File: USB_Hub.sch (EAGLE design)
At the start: 53 parts, among them CON1 USB-ZX62, CON2 USB-5075AR-04-WH, CON3 USB-5075AR-04-WH, CON4 USB-5075AR-04-WH, CON5 USB-5075AR-04-WH, IC1 UPC720115, IC2 AP22652, J1 VBUS, J2 BUS/SELF, SW1 RESET, X1 24MHz

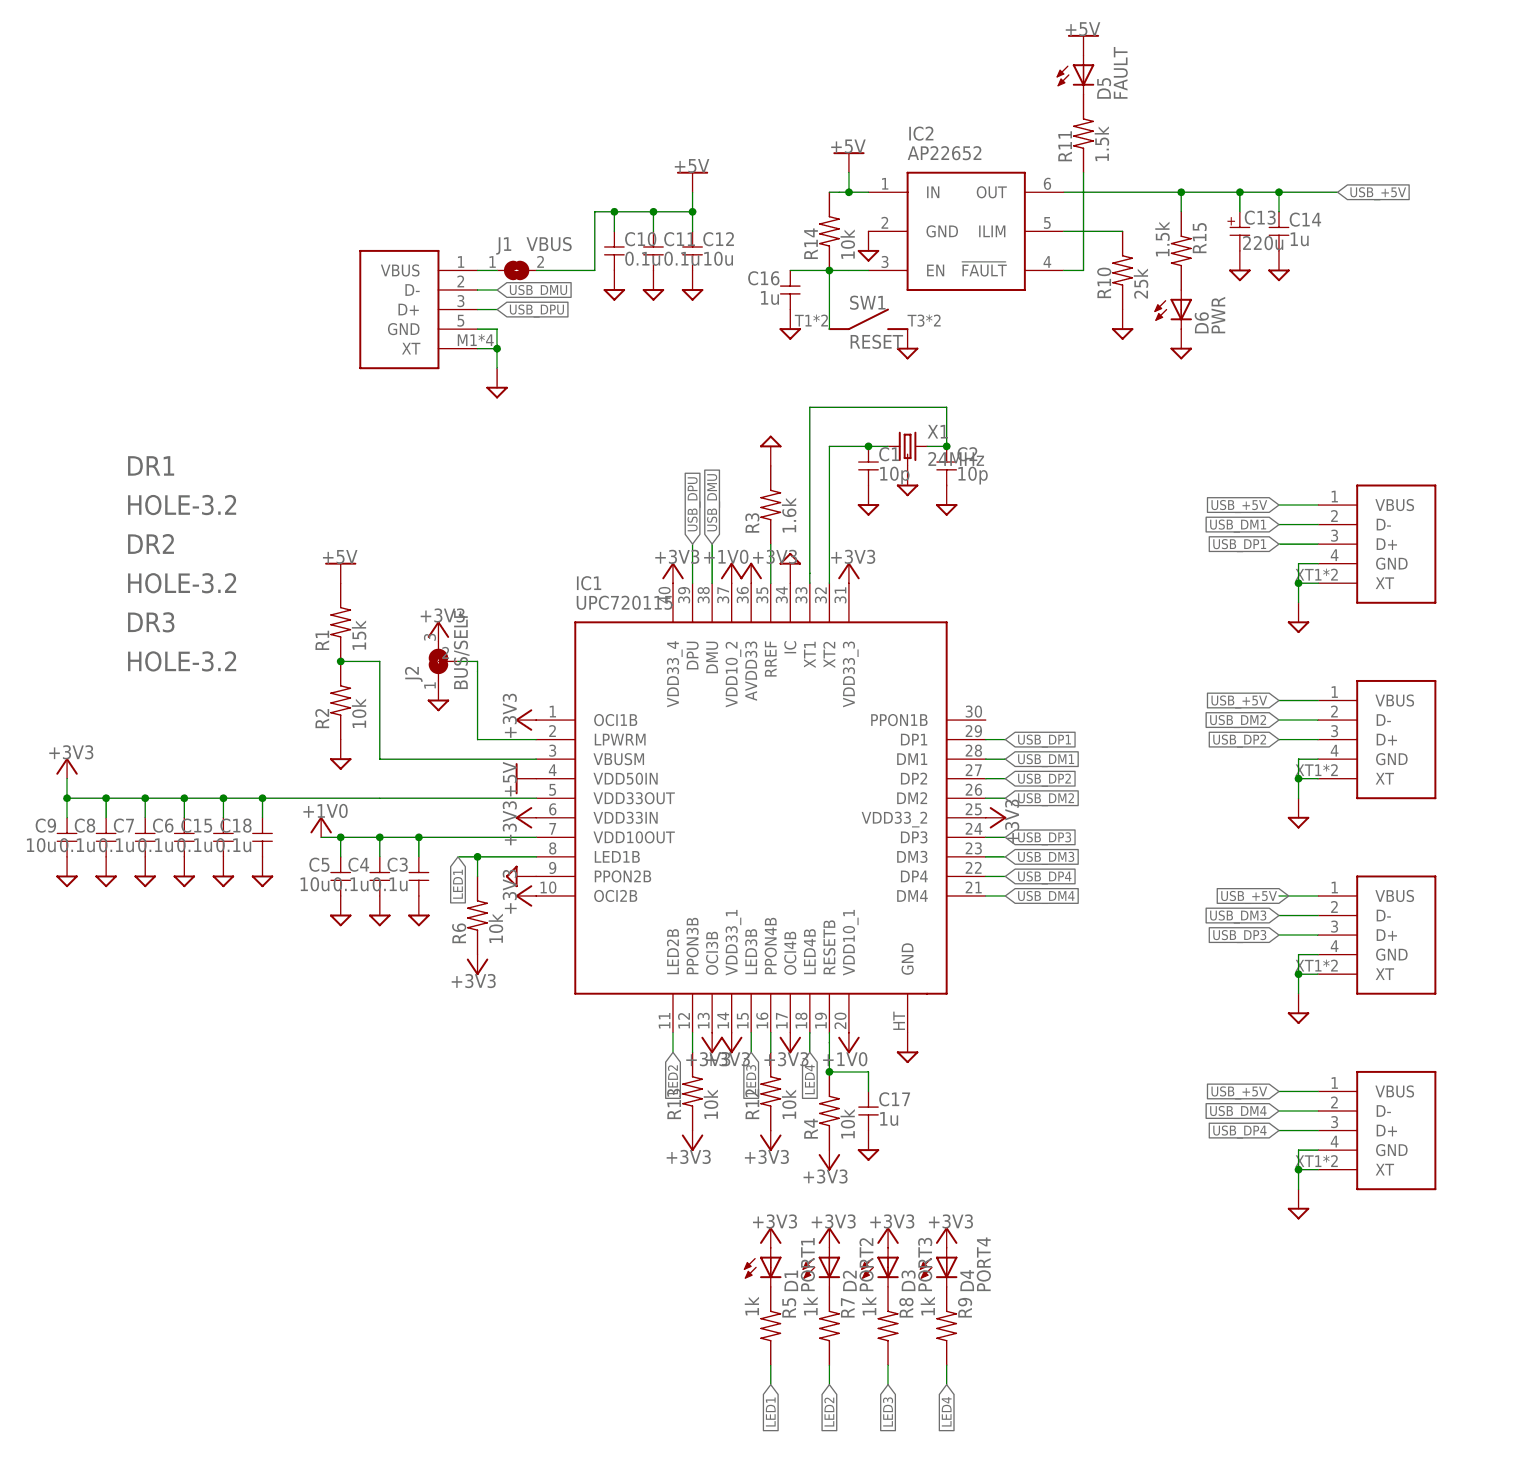
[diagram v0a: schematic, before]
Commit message: 電圧確認用のポートを追加
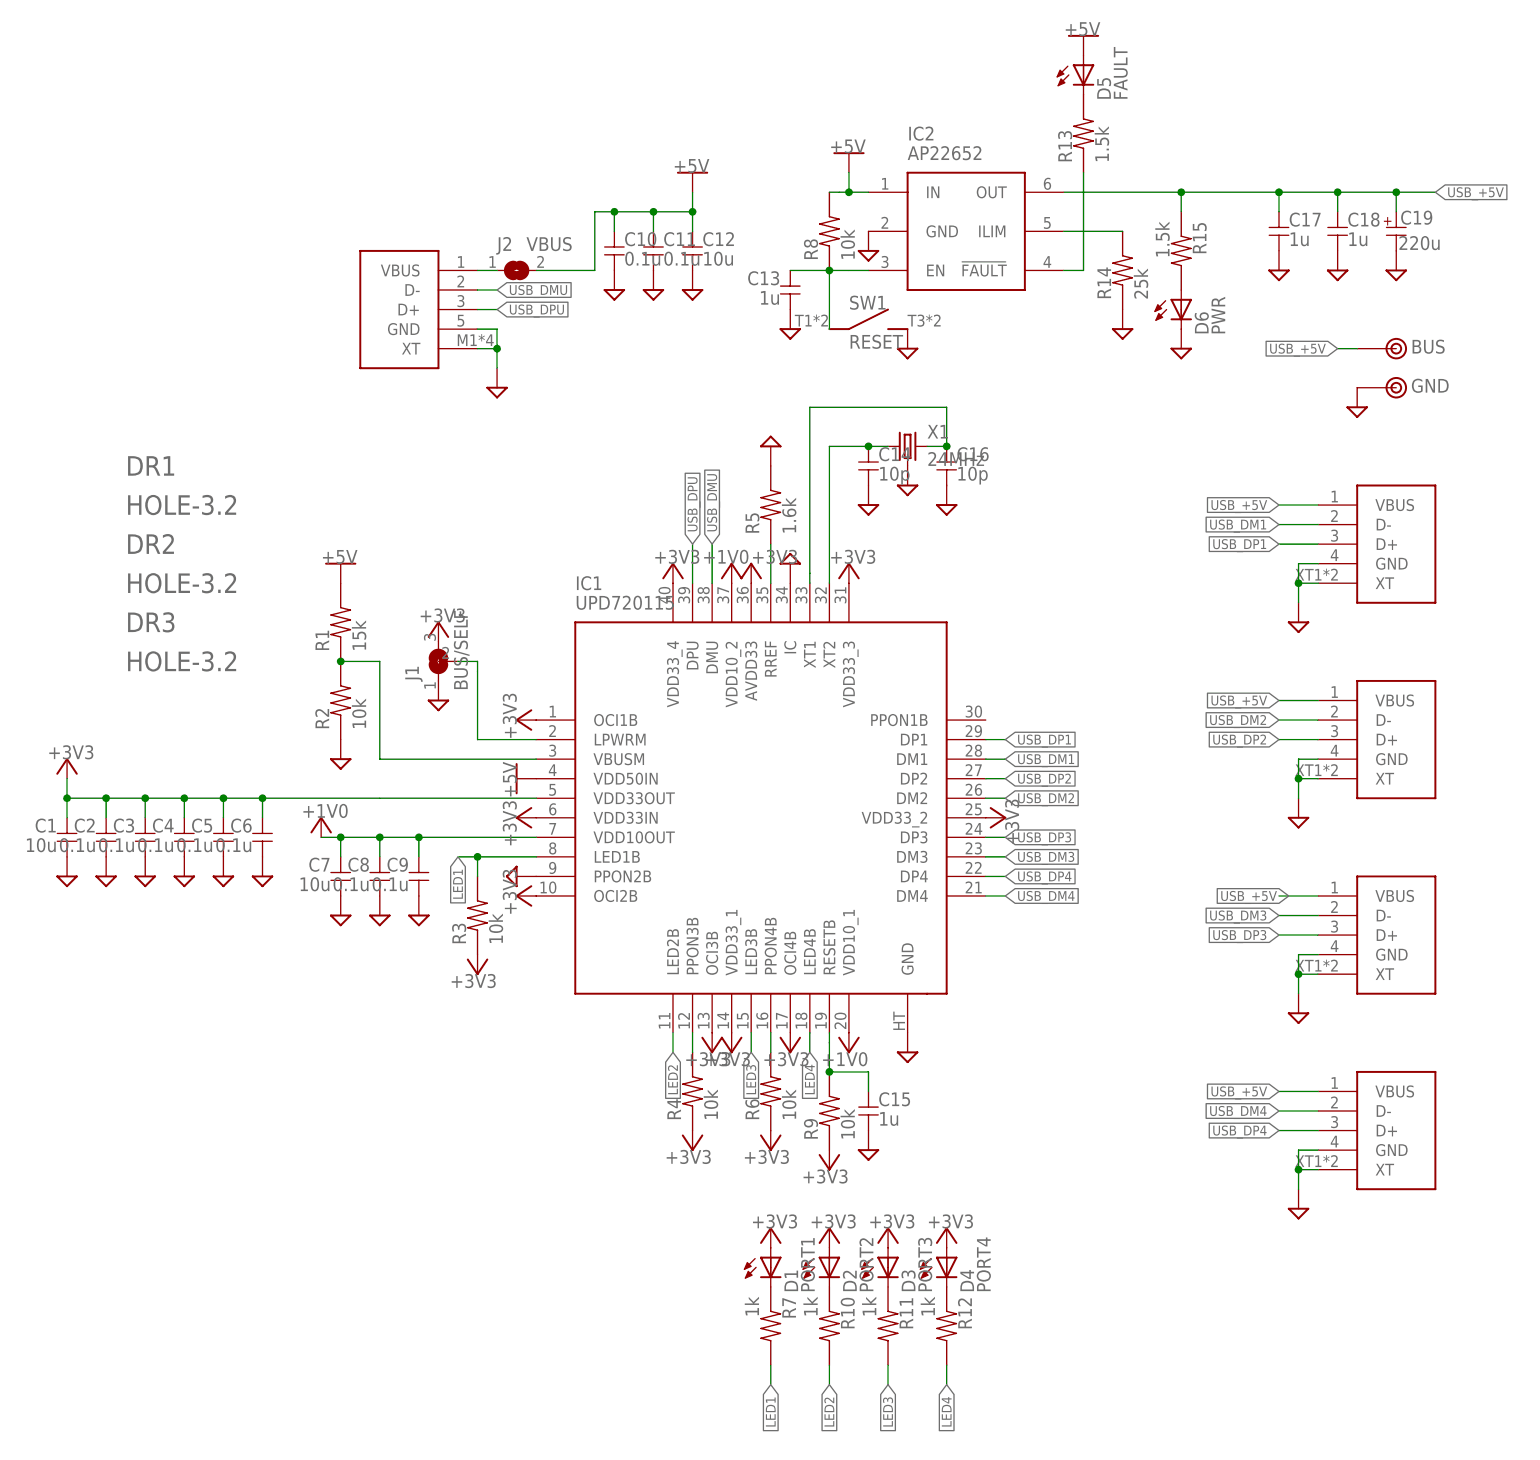
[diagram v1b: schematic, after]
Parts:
- added C19: 220u, my_rcl:CPOLE2.5-6.5
- added TP1: BUS, my_connector:TESTPIN
- added TP2: GND, my_connector:TESTPIN
- C1: value 10p -> 10u
- C13: value 220u -> 1u; device my_rcl:CPOLE2.5-6.5 -> my_rcl:C-1608
- C14, C16: value 1u -> 10p
- C15, C18: value 0.1u -> 1u
- C2: value 10p -> 0.1u
- C5, C9: value 10u -> 0.1u
- C7: value 0.1u -> 10u
- D1, D2, D3, D4: device my_rcl:LED-SMD1608 -> my_rcl:LED-2.5
- IC1: value UPC720115 -> UPD720115; device my_ic:UPC720115 -> my_ic:UPD720115
- J1: value VBUS -> BUS/SELF; device my_rcl:SJ-2012 -> my_rcl:SJ-3-1608
- J2: value BUS/SELF -> VBUS; device my_rcl:SJ-3-1608 -> my_rcl:SJ-2012
- R10: value 25k -> 1k
- R11: value 1.5k -> 1k
- R12: value 10k -> 1k
- R13: value 10k -> 1.5k
- R14: value 10k -> 25k
- R3: value 1.6k -> 10k
- R5: value 1k -> 1.6k
- R8, R9: value 1k -> 10k
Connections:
- net +1V0: now also C7.1, C8.1, C9.1; no longer C3.1, C4.1, C5.1
- net +3V3: now also C1.1, C2.1, C3.1, C4.1, C5.1, J1.3, R3.1, R9.1; no longer C15.1, C18.1, C7.1, C8.1, C9.1, J2.3, R12.1, R13.1
- net +5V: now also J2.2, R8.2; no longer J1.2, R14.2
- net GND: now also C19.2, J1.1, R14.1, R5.2, TP2.1; no longer J2.1, R10.1, R3.2
- net LED1: now also R3.2, R7.2; no longer R5.2, R6.2
- net LED2: now also R10.2; no longer R7.2
- net LED3: now also R11.2; no longer R8.2
- net LED4: now also R12.2; no longer R9.2
- net N$1: now also J2.1; no longer J1.1
- net N$10: now also R11.1; no longer R8.1
- net N$11: now also R12.1; no longer R9.1
- net N$12: now also R13.1; no longer R11.1
- net N$13: now also R14.2; no longer R10.2
- net N$14: now also R6.2; no longer R12.2
- net N$15: now also R4.2; no longer R13.2
- net N$17: now also J1.2; no longer J2.2
- net N$2: now also R13.2; no longer R11.2
- net N$4: now also R5.1; no longer R3.1
- net N$5: now also C14.1; no longer C1.1
- net N$6: now also C16.1; no longer C2.1
- net N$7: now also C15.1, R9.2; no longer C17.1, R4.2
- net N$8: now also R7.1; no longer R5.1
- net N$9: now also R10.1; no longer R7.1
- net USB_+5V: now also C17.1, C18.1, C19.1, TP1.1; no longer C13.1, C14.1
- net VBUS_EN: now also C13.1, R8.1; no longer C16.1, R14.1
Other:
- moved on the sheet: C1, C14, C15, C16, C17, C18, C2, C3, C4, C5, C6, C7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
